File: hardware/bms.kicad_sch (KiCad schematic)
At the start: 28 parts, among them U5 MAX77751, U6 LM75B, U7 MAX17048G

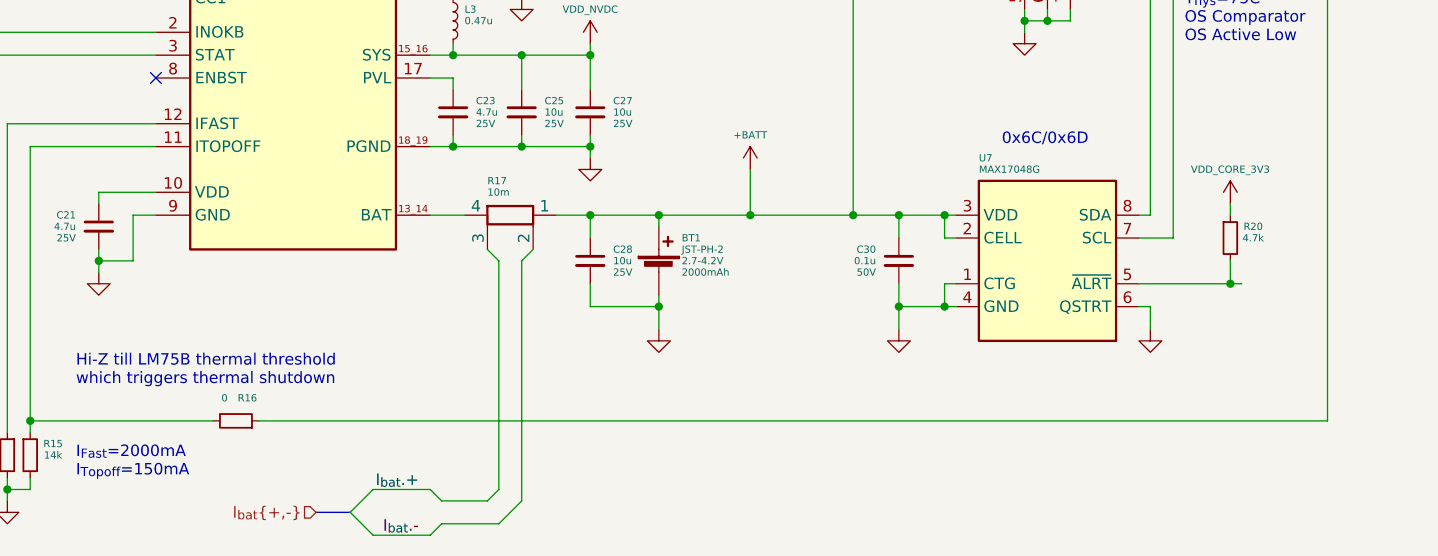
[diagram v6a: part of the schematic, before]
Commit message: initial component placement and design simplification
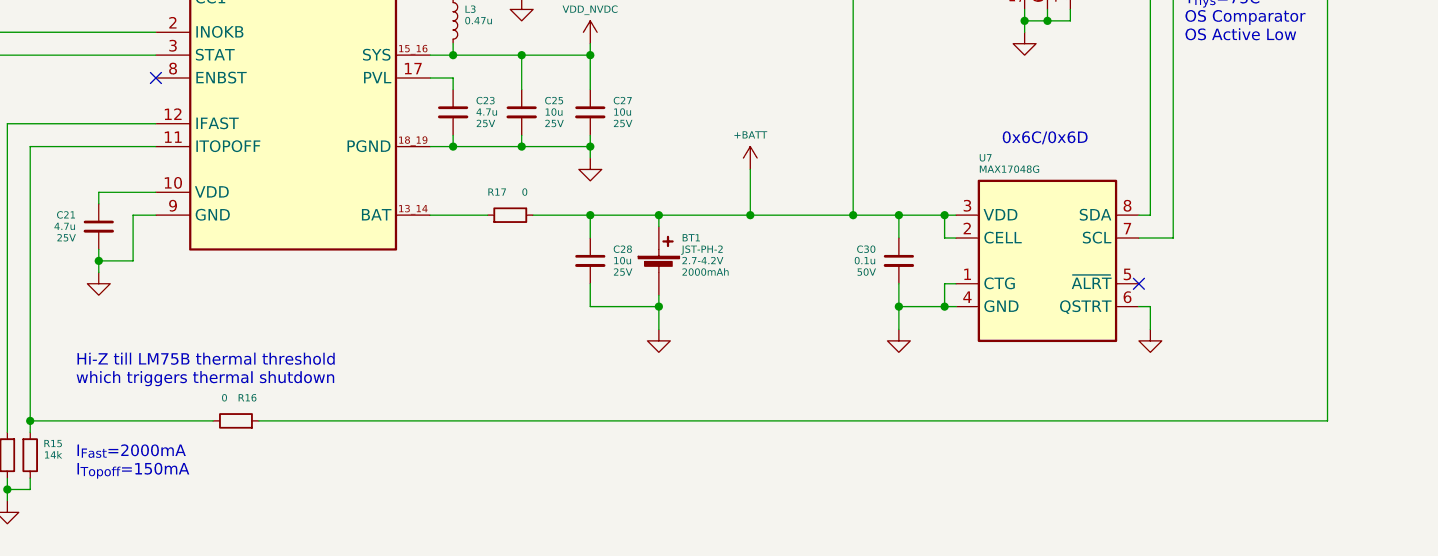
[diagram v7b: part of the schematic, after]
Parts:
- removed R17: 10m, Resistor_SMD:R_0603_1608Metric_Pad0.98x0.95mm_HandSolder, symbol Device:R_Shunt
- removed R20: 4.7k, Resistor_SMD:R_0402_1005Metric, symbol Device:R_Small
- added R17: 0, Resistor_SMD:R_0603_1608Metric_Pad0.98x0.95mm_HandSolder, symbol Device:R_Small
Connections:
- net +BATT: now also R17.2
- net at U5.13_14 (BAT): now also R17.1
- no-connect marks 1 -> 2
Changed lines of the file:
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@@
   (junction (at 129.54 67.31) (diameter 0) (color 0 0 0 0)
   )
-  (junction (at 215.9 100.33) (diameter 0) (color 0 0 0 0)
-  )
   (junction (at 177.8 54.61) (diameter 0) (color 0 0 0 0)
   )
@@
   )
   (no_connect (at 96.52 77.47))
-  (bus_entry (at 118.11 125.73) (size 2.54 2.54)
-    (stroke (width 0) (type default) (color 0 0 0 0))
-  )
-  (bus_entry (at 118.11 125.73) (size 2.54 -2.54)
-    (stroke (width 0) (type default) (color 0 0 0 0))
-  )
+  (no_connect (at 205.74 100.33))
   (bus_entry (at 229.87 54.61) (size -2.54 2.54)
     (stroke (width 0) (type default) (color 0 0 0 0))
@@
     (stroke (width 0) (type default) (color 0 0 0 0))
   )
-  (wire (pts (xy 215.9 97.79) (xy 215.9 100.33))
-    (stroke (width 0) (type default) (color 0 0 0 0))
-  )
   (wire (pts (xy 152.4 92.71) (xy 162.56 92.71))
     (stroke (width 0) (type default) (color 0 0 0 0))
@@
     (stroke (width 0) (type default) (color 0 0 0 0))
   )
-  (wire (pts (xy 140.97 92.71) (xy 144.78 92.71))
+  (wire (pts (xy 138.43 92.71) (xy 144.78 92.71))
     (stroke (width 0) (type default) (color 0 0 0 0))
   )
@@
     (stroke (width 0) (type default) (color 0 0 0 0))
   )
-  (wire (pts (xy 127 123.19) (xy 128.27 124.46))
-    (stroke (width 0) (type default) (color 0 0 0 0))
-  )
   (wire (pts (xy 127 74.93) (xy 129.54 74.93))
     (stroke (width 0) (type default) (color 0 0 0 0))
@@
     (stroke (width 0) (type default) (color 0 0 0 0))
   )
-  (wire (pts (xy 134.62 127) (xy 137.16 124.46))
-    (stroke (width 0) (type default) (color 0 0 0 0))
-  )
   (wire (pts (xy 137.16 55.88) (xy 144.78 55.88))
     (stroke (width 0) (type default) (color 0 0 0 0))
@@
     (stroke (width 0) (type default) (color 0 0 0 0))
   )
-  (bus (pts (xy 118.11 125.73) (xy 114.3 125.73))
-    (stroke (width 0) (type default) (color 0 0 0 0))
-  )
   (wire (pts (xy 73.66 64.77) (xy 73.66 83.82))
     (stroke (width 0) (type default) (color 0 0 0 0))
@@
     (stroke (width 0) (type default) (color 0 0 0 0))
   )
-  (wire (pts (xy 134.62 97.79) (xy 134.62 123.19))
-    (stroke (width 0) (type default) (color 0 0 0 0))
-  )
   (wire (pts (xy 205.74 57.15) (xy 209.55 57.15))
     (stroke (width 0) (type default) (color 0 0 0 0))
@@
     (stroke (width 0) (type default) (color 0 0 0 0))
   )
-  (wire (pts (xy 127 128.27) (xy 120.65 128.27))
-    (stroke (width 0) (type default) (color 0 0 0 0))
-  )
   (wire (pts (xy 207.01 102.87) (xy 205.74 102.87))
     (stroke (width 0) (type default) (color 0 0 0 0))
@@
     (stroke (width 0) (type default) (color 0 0 0 0))
   )
-  (wire (pts (xy 137.16 97.79) (xy 138.43 96.52))
-    (stroke (width 0) (type default) (color 0 0 0 0))
-  )
   (wire (pts (xy 66.04 74.93) (xy 96.52 74.93))
     (stroke (width 0) (type default) (color 0 0 0 0))
@@
     (stroke (width 0) (type default) (color 0 0 0 0))
   )
-  (wire (pts (xy 137.16 97.79) (xy 137.16 124.46))
-    (stroke (width 0) (type default) (color 0 0 0 0))
-  )
   (wire (pts (xy 185.42 62.23) (xy 177.8 62.23))
     (stroke (width 0) (type default) (color 0 0 0 0))
@@
     (stroke (width 0) (type default) (color 0 0 0 0))
   )
-  (wire (pts (xy 134.62 123.19) (xy 133.35 124.46))
-    (stroke (width 0) (type default) (color 0 0 0 0))
-  )
   (wire (pts (xy 129.54 67.31) (xy 129.54 66.04))
     (stroke (width 0) (type default) (color 0 0 0 0))
@@
     (stroke (width 0) (type default) (color 0 0 0 0))
   )
-  (wire (pts (xy 205.74 100.33) (xy 215.9 100.33))
-    (stroke (width 0) (type default) (color 0 0 0 0))
-  )
   (wire (pts (xy 129.54 77.47) (xy 127 77.47))
     (stroke (width 0) (type default) (color 0 0 0 0))
@@
     (stroke (width 0) (type default) (color 0 0 0 0))
   )
-  (wire (pts (xy 215.9 91.44) (xy 215.9 92.71))
-    (stroke (width 0) (type default) (color 0 0 0 0))
-  )
-  (wire (pts (xy 128.27 127) (xy 134.62 127))
-    (stroke (width 0) (type default) (color 0 0 0 0))
-  )
   (bus (pts (xy 81.28 62.23) (xy 81.28 63.5))
     (stroke (width 0) (type default) (color 0 0 0 0))
@@
     (stroke (width 0) (type default) (color 0 0 0 0))
   )
-  (wire (pts (xy 127 123.19) (xy 120.65 123.19))
-    (stroke (width 0) (type default) (color 0 0 0 0))
-  )
   (wire (pts (xy 179.07 105.41) (xy 179.07 102.87))
     (stroke (width 0) (type default) (color 0 0 0 0))
@@
     (stroke (width 0) (type default) (color 0 0 0 0))
   )
-  (wire (pts (xy 133.35 96.52) (xy 134.62 97.79))
-    (stroke (width 0) (type default) (color 0 0 0 0))
-  )
-  (wire (pts (xy 128.27 127) (xy 127 128.27))
-    (stroke (width 0) (type default) (color 0 0 0 0))
-  )
-  (wire (pts (xy 217.17 100.33) (xy 215.9 100.33))
-    (stroke (width 0) (type default) (color 0 0 0 0))
-  )
-  (wire (pts (xy 128.27 124.46) (xy 133.35 124.46))
-    (stroke (width 0) (type default) (color 0 0 0 0))
-  )
   (wire (pts (xy 208.28 43.18) (xy 208.28 44.45))
     (stroke (width 0) (type default) (color 0 0 0 0))
   )
-  (wire (pts (xy 130.81 92.71) (xy 127 92.71))
+  (wire (pts (xy 127 92.71) (xy 133.35 92.71))
     (stroke (width 0) (type default) (color 0 0 0 0))
   )
@@
     (effects (font (size 1.27 1.27)) (justify left bottom))
   )
-  (label "I_{bat}.-" (at 125.73 128.27 180)
-    (effects (font (size 1.27 1.27)) (justify right bottom))
-  )
   (label "USB_CHG.D+" (at 83.82 59.69 0)
     (effects (font (size 0.8 0.8)) (justify left bottom))
@@
     (effects (font (size 0.8 0.8)) (justify left bottom))
   )
-  (label "I_{bat}.+" (at 125.73 123.19 180)
-    (effects (font (size 1.27 1.27)) (justify right bottom))
-  )
   (label "USB_CC.1" (at 83.82 68.58 0)
     (effects (font (size 0.8 0.8)) (justify left bottom))
@@
   (hierarchical_label "USB_CC{1 2}" (shape bidirectional) (at 78.74 60.96 180)
     (effects (font (size 0.8 0.8)) (justify right))
-  )
-  (hierarchical_label "I_{bat}{+,-}" (shape input) (at 114.3 125.73 180)
-    (effects (font (size 1.27 1.27)) (justify right))
   )
   (hierarchical_label "POWER_GOOD" (shape output) (at 58.42 72.39 180)
@@
     (pin "8")
   )
-  (symbol (lib_id "Device:R_Shunt") (at 135.89 92.71 270) (unit 1)
-    (in_bom yes) (on_board yes)
-    (property "Reference" "R17" (id 0) (at 133.35 88.9 90)
-      (effects (font (size 0.8 0.8)) (justify left))
-    )
-    (property "Value" "10m" (id 1) (at 133.35 90.17 90)
-      (effects (font (size 0.8 0.8)) (justify left))
-    )
-    (property "Footprint" "Resistor_SMD:R_0603_1608Metric_Pad0.98x0.95mm_HandSolder" (id 2) (at 135.89 90.932 90)
-      (effects (font (size 1.27 1.27)) hide)
-    )
-    (property "Datasheet" "~" (id 3) (at 135.89 92.71 0)
-      (effects (font (size 1.27 1.27)) hide)
-    )
-    (pin "1")
-    (pin "2")
-    (pin "3")
-    (pin "4")
-  )
   (symbol (lib_id "power:GND") (at 88.9 53.34 0) (unit 1)
     (in_bom yes) (on_board yes) (fields_autoplaced)
@@
     (pin "2")
   )
+  (symbol (lib_id "Device:R_Small") (at 135.89 92.71 90) (unit 1)
+    (in_bom yes) (on_board yes)
+    (property "Reference" "R17" (id 0) (at 133.35 90.17 90)
+      (effects (font (size 0.8 0.8)) (justify right))
+    )
+    (property "Value" "0" (id 1) (at 137.16 90.17 90)
+      (effects (font (size 0.8 0.8)) (justify right))
+    )
+    (property "Footprint" "Resistor_SMD:R_0603_1608Metric_Pad0.98x0.95mm_HandSolder" (id 2) (at 135.89 92.71 0)
+      (effects (font (size 0.8 0.8)) hide)
+    )
+    (property "Datasheet" "~" (id 3) (at 135.89 92.71 0)
+      (effects (font (size 0.8 0.8)) hide)
+    )
+    (pin "1")
+    (pin "2")
+  )
   (symbol (lib_id "Device:C_Small") (at 129.54 63.5 0) (unit 1)
     (in_bom yes) (on_board yes)
@@
     (pin "1")
     (pin "2")
-  )
-  (symbol (lib_id "bt_power:VDD_CORE_3V3") (at 215.9 91.44 0) (unit 1)
-    (in_bom no) (on_board no)
-    (property "Reference" "#U09" (id 0) (at 216.4334 91.44 0)
-      (effects (font (size 1.27 1.27)) hide)
-    )
-    (property "Value" "VDD_CORE_3V3" (id 1) (at 215.9 87.63 0)
-      (effects (font (size 0.8 0.8)))
-    )
-    (property "Footprint" "" (id 2) (at 216.4334 91.44 0)
-      (effects (font (size 1.27 1.27)) hide)
-    )
-    (property "Datasheet" "" (id 3) (at 216.4334 91.44 0)
-      (effects (font (size 1.27 1.27)) hide)
-    )
-    (pin "1")
   )
   (symbol (lib_id "Device:C_Small") (at 129.54 81.28 0) (unit 1)
@@
       (effects (font (size 0.8 0.8)) hide)
     )
-    (pin "1")
-    (pin "2")
-  )
-  (symbol (lib_id "Device:R_Small") (at 215.9 95.25 0) (unit 1)
-    (in_bom yes) (on_board yes)
-    (property "Reference" "R20" (id 0) (at 218.44 93.98 0)
-      (effects (font (size 0.8 0.8)))
-    )
-    (property "Value" "4.7k" (id 1) (at 218.44 95.25 0)
-      (effects (font (size 0.8 0.8)))
-    )
-    (property "Footprint" "Resistor_SMD:R_0402_1005Metric" (id 2) (at 215.9 95.25 0)
-      (effects (font (size 0.8 0.8)) hide)
-    )
-    (property "Datasheet" "~" (id 3) (at 215.9 95.25 0)
-      (effects (font (size 0.8 0.8)) hide)
-    )

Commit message: fixing submodule
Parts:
- added Q1: Q_NMOS_DGS, Package_TO_SOT_SMD:SOT-323_SC-70, symbol Device:Q_NMOS_DGS
- added R21: 1k, Resistor_SMD:R_0402_1005Metric, symbol Device:R_Small
- added TP1: SNS_BAT-, symbol Connector:TestPoint
- added TP2: SNS_BAT+, symbol Connector:TestPoint
- D2: Label STAT -> PGOOD
- D3: Label PGOOD -> STAT
- R12: value 1k -> 100k
- R17: footprint Resistor_SMD:R_0603_1608Metric_Pad0.98x0.95mm_HandSolder -> Resistor_SMD:R_0805_2012Metric
- U5: footprint bt_Package_QFN:FC2QFN-24-3x3_P0.4mm -> Package_QFN_bt:FC2QFN-24-3x3_P0.4mm
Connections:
- net +BATT: now also TP2.1
- net 3V3_CORE: no longer D2.2 (A), D3.2 (A), R11.2
- net GND: now also Q1.3 (S)
- net at R13.1: now also R11.1, U5.2 (INOKB), Q1.2 (G); no longer D2.1 (K)
- net at U5.3 (STAT): now also R21.1; no longer R13.2
- net at R17.1, U5.13_14 (BAT): now also TP1.1
- net at D3.1 (K): now also R21.2; no longer R12.1
- removed net POWER_GOOD: R11.1, R12.2, U5.2 (INOKB)
- new net: D2.1 (K), R13.2
- new net USB_POWER_GOOD: Q1.1 (D), R12.1
- new net VDD_USB_3V3: D2.2 (A), D3.2 (A), R11.2, R12.2
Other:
- note removed: "DEBUG LEDS"
- moved on the sheet: R11
